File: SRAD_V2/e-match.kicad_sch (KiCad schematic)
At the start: 37 parts, among them IC1 NCV81071BZR2G, IC2 NCV81071BZR2G, Q1 NTMFS5C673NT1G, Q2 NTMFS5C673NT1G, Q3 NTMFS5C673NT1G, Q4 NTMFS5C673NT1G, U3 TMCS1108A2UQDR

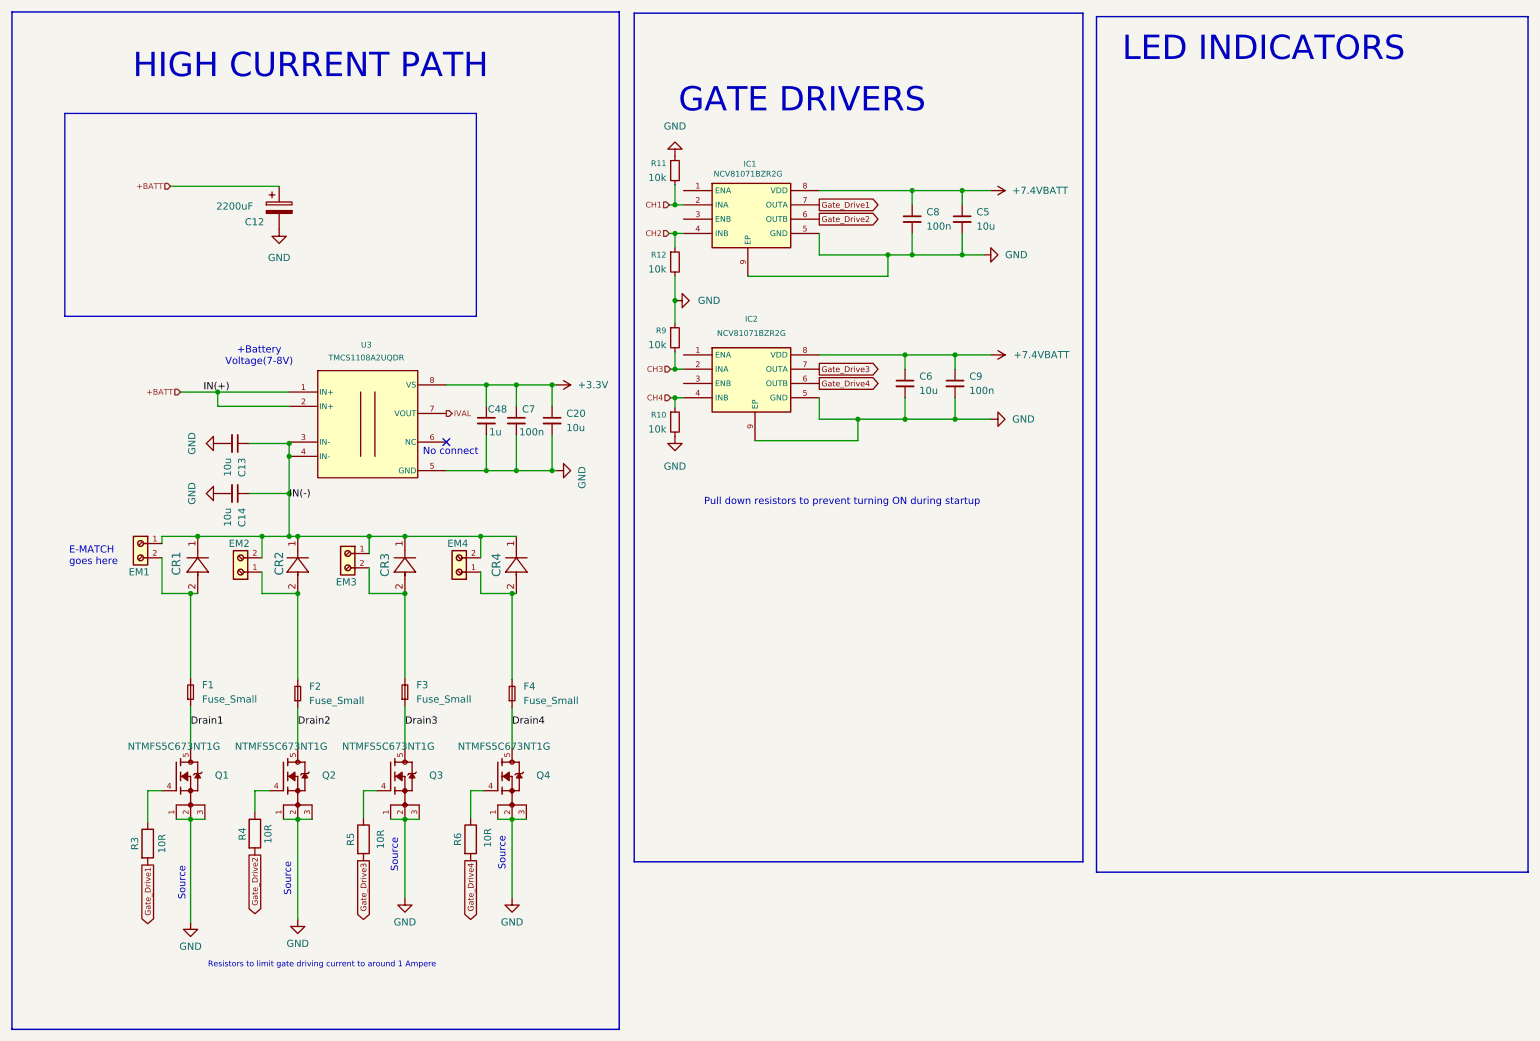
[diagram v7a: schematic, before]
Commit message: Merged the new schematic with the main project successfully!
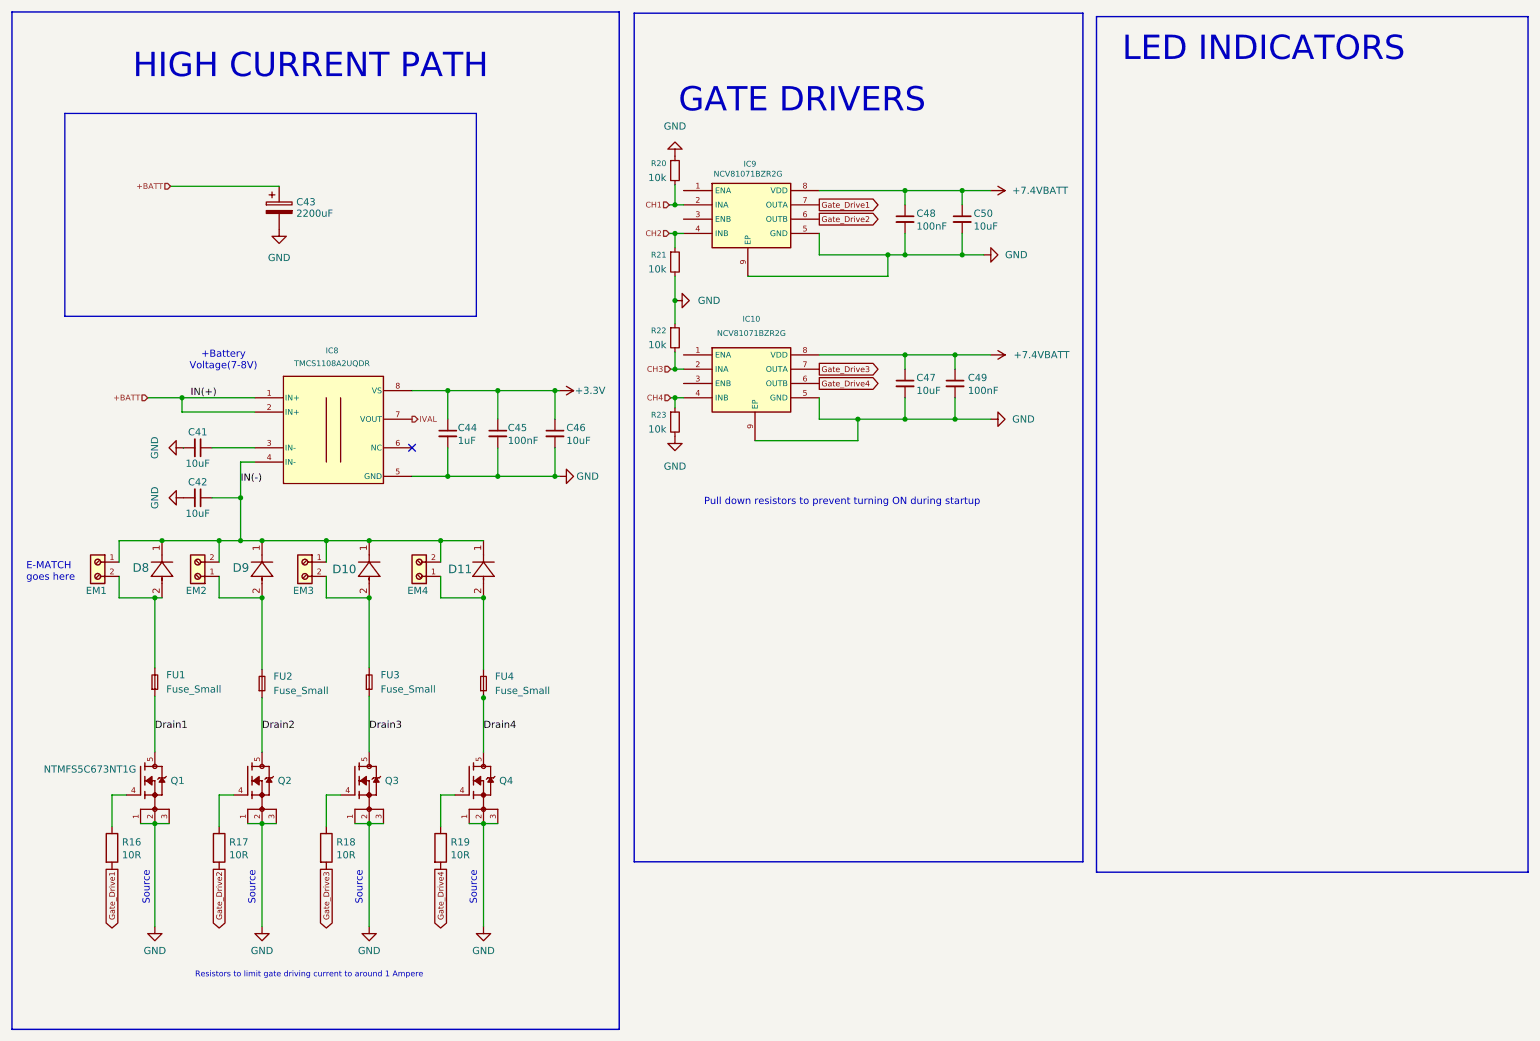
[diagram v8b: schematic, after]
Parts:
- C41: renamed from C13; value 10u -> 10uF
- C42: renamed from C14; value 10u -> 10uF
- C44: renamed from C48; value 1u -> 1uF
- C45: renamed from C7; value 100n -> 100nF
- C46: renamed from C20; value 10u -> 10uF
- C47: renamed from C6; value 10u -> 10uF
- C48: renamed from C8; value 100n -> 100nF
- C49: renamed from C9; value 100n -> 100nF
- C50: renamed from C5; value 10u -> 10uF
- renumbered C12 to C43, CR3 to D10, CR4 to D11, CR1 to D8, CR2 to D9, F1 to FU1, F2 to FU2, F3 to FU3, F4 to FU4, IC2 to IC10, U3 to IC8, IC1 to IC9, R3 to R16, R4 to R17, R5 to R18, R6 to R19, R11 to R20, R12 to R21, R9 to R22, R10 to R23
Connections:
- net IN(-): no longer C41.1, IC8.3 (IN-)
- new net: C41.1, IC8.3 (IN-)
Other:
- note removed: "No connect"
- moved on the sheet: C41, C42, C44, C45, C46, C48, D10, D11, D8, D9, EM1, EM2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
